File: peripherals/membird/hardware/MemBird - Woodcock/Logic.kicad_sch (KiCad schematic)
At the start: 25 parts, among them U10 74LS393, U11 74LVC1G06, U12 74LVC1G06, U3 74HC14, U4 74HC86, U5 74HC20, U6 74HC139, U7 74HC32, U8 74HC32, U9 74LVC1G14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

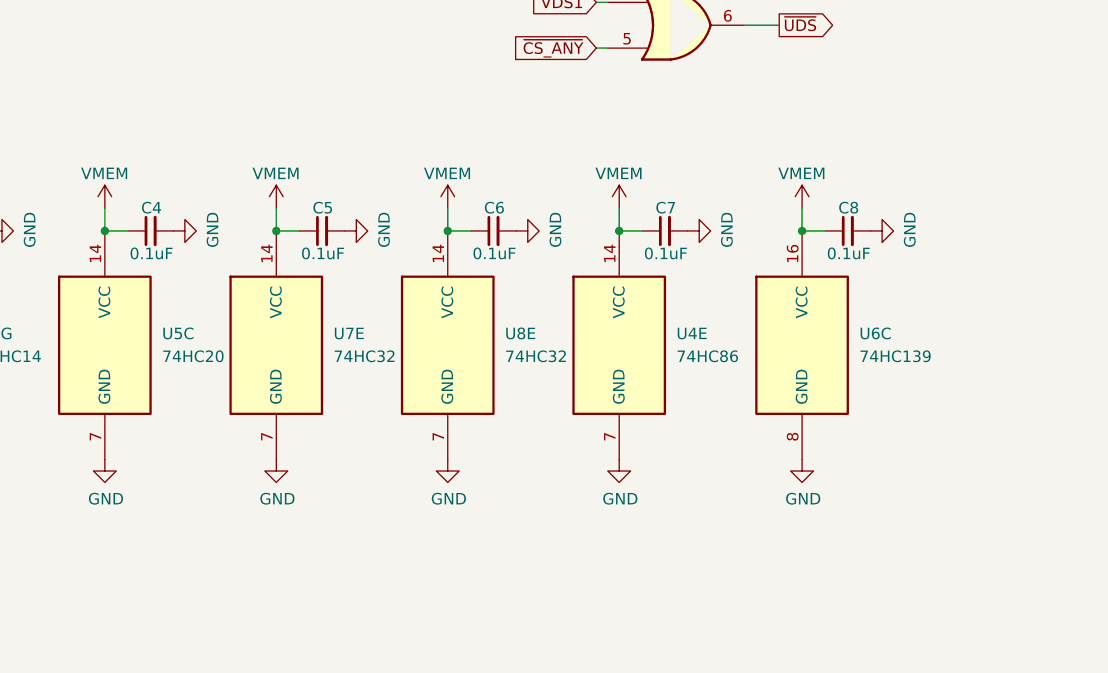
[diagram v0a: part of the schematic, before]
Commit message: Finished the MemBird - Woodcock 16-bit memory board layout
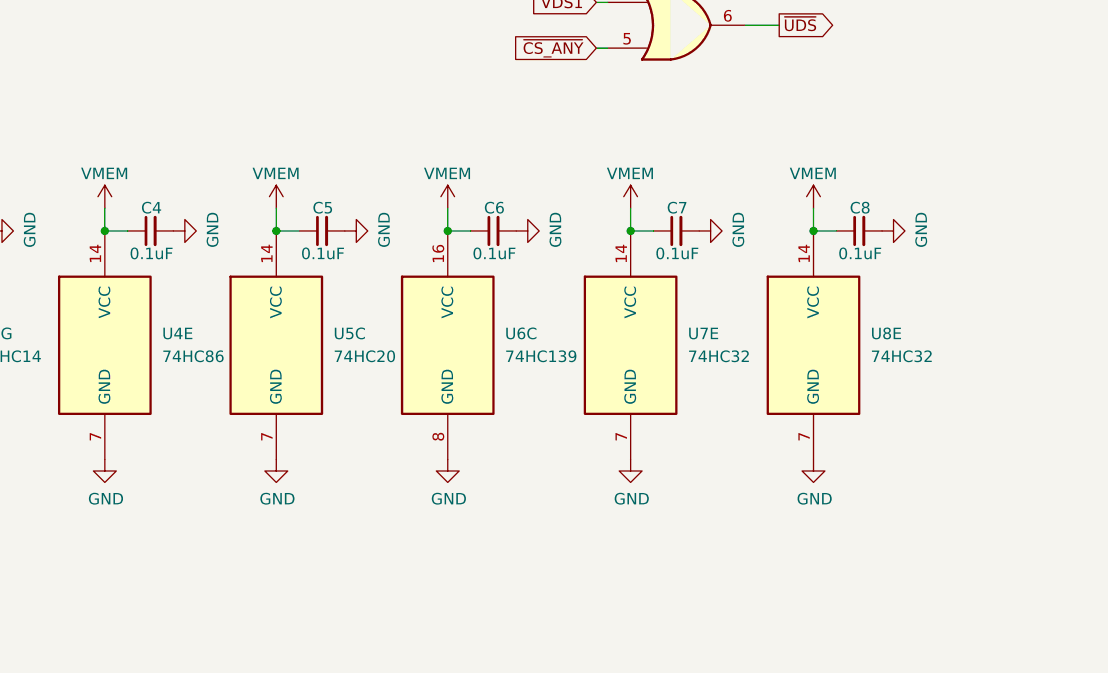
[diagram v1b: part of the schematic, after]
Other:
- moved on the sheet: C7, C8, U4E, U5C, U6C, U7E, U8E

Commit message: k30p-VME rev.1, MemBird Woodcock rev.1, and frontpanels
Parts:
- added JP6: /2, Jumper:SolderJumper-2_P1.3mm_Open_RoundedPad1.0x1.5mm, symbol Jumper:SolderJumper_2_Open
- added JP7: /4, Jumper:SolderJumper-2_P1.3mm_Bridged_RoundedPad1.0x1.5mm, symbol Jumper:SolderJumper_2_Bridged
- added JP8: /8, Jumper:SolderJumper-2_P1.3mm_Open_RoundedPad1.0x1.5mm, symbol Jumper:SolderJumper_2_Open
- added JP9: /16, Jumper:SolderJumper-2_P1.3mm_Open_RoundedPad1.0x1.5mm, symbol Jumper:SolderJumper_2_Open
- U10: value 74LS393 -> 74HC393
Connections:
- net at JP4.1 (A), U12.2: now also JP6.2 (B), JP7.2 (B), JP8.2 (B), JP9.2 (B); no longer U10.4 (Q1)
- net at U10.3 (Q0): now also JP6.1 (A)
- net at U10.5 (Q2): now also JP8.1 (A)
- net at U10.6 (Q3): now also JP9.1 (A)
- new net: JP7.1 (A), U10.4 (Q1)
- no-connect marks 23 -> 20
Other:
- note removed: "TODO: if you did MD32, you'd have two more 16-bit transcievers (these are using positive logic, so need to be translated) B0OE <- CS_ANY & (!LWORD & !A1 | LWORD) & DS0 B1OE <- CS_ANY & (!LWORD & !A1 | LWORD) & DS1 B2LOE <- CS_ANY & !LWORD & A1 & DS0 B3LOE <- CS_ANY & !LWORD & A1 & DS1 B2UOE <- CS_ANY & LWORD B3UOE <- CS_ANY & LWORD"
- moved on the sheet: C11, U10C
